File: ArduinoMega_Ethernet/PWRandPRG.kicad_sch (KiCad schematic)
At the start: 71 parts, among them J1 RJ45_Amphenol_RJMG1BD3B8K1ANR, J11 Micro_SD_Card_Det_Hirose_DM3AT, J9 PROGRAM_POWER_USBC, U2 CH340C, U3 ISM330DHCX, U4 W5500, U5 LM3281, U6 74HC244, U7 SE050C2HQ1, Y2 25Mhz

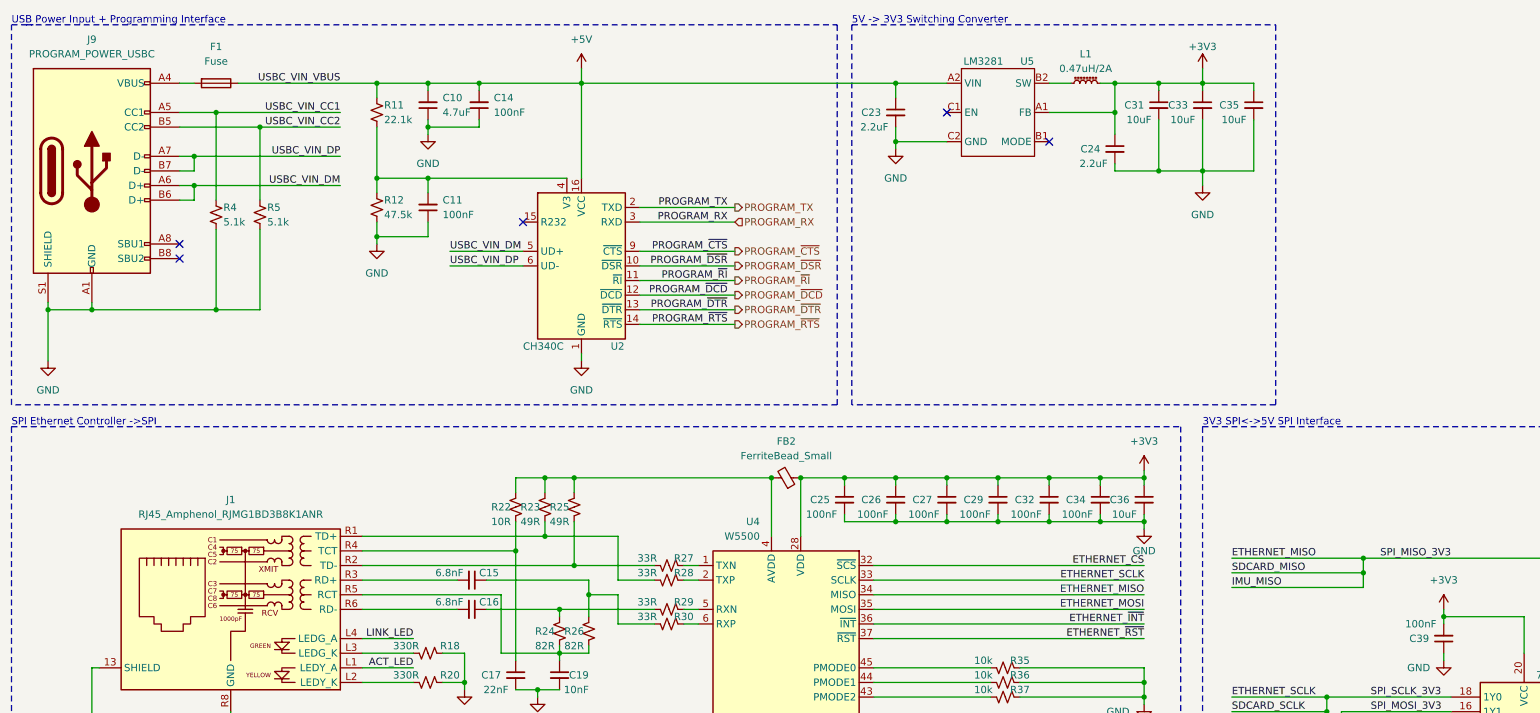
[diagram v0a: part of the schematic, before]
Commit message: add usb protection, fix ioref
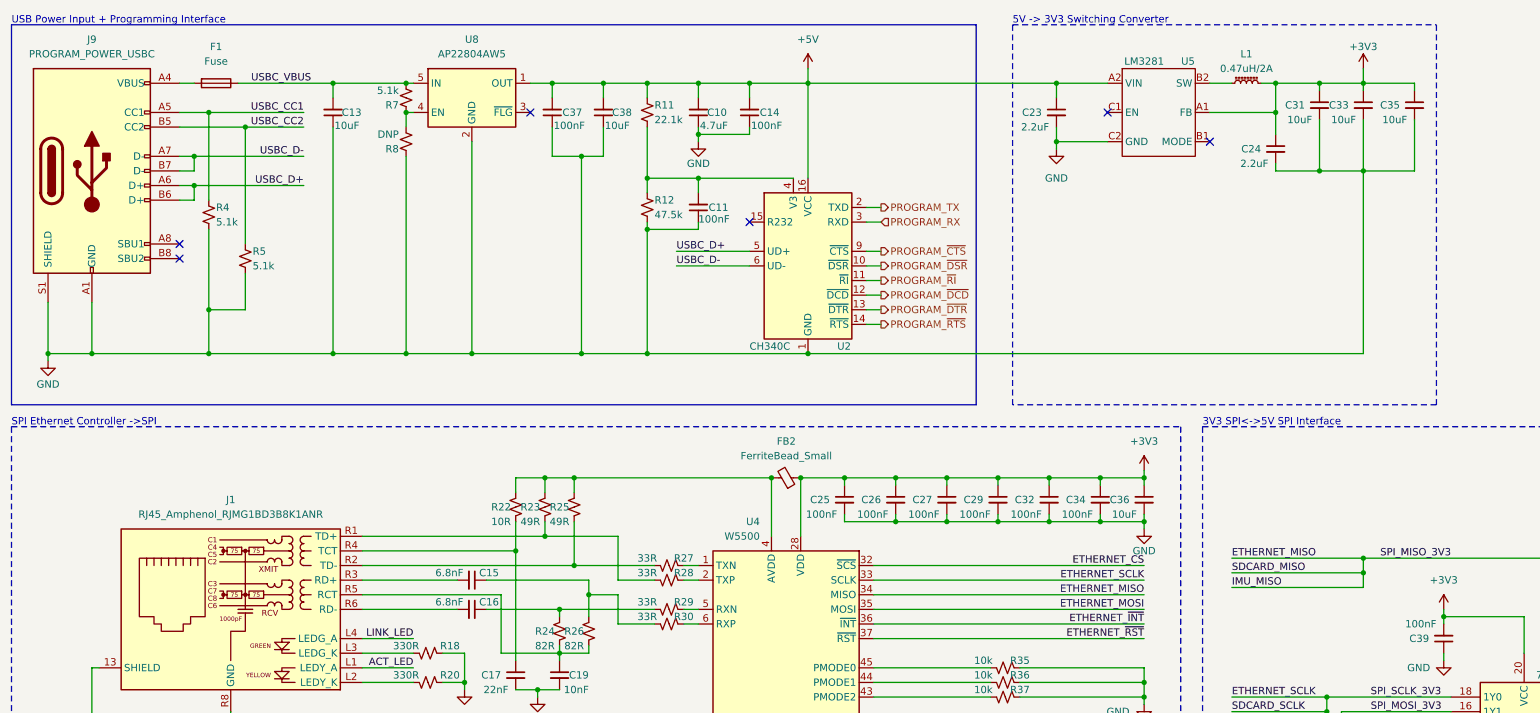
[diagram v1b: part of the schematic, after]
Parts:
- added C13, C38: 10uF, Capacitor_SMD:C_0805_2012Metric_Pad1.18x1.45mm_HandSolder, symbol Device:C_Small
- added C37: 100nF, Capacitor_SMD:C_0603_1608Metric, symbol Device:C_Small
- added R7: 5.1k, Resistor_SMD:R_0603_1608Metric, symbol Device:R_Small_US
- added R8: DNP, Resistor_SMD:R_0603_1608Metric, symbol Device:R_Small_US
- added U8: AP22804AW5, Package_TO_SOT_SMD:SOT-23-5, symbol Power_Management:AP22804AW5
- C31, C33, C35, C36: footprint Capacitor_SMD:C_1206_3216Metric -> Capacitor_SMD:C_0805_2012Metric_Pad1.18x1.45mm_HandSolder
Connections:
- net +5V: now also C37.2, C38.2, U8.1 (OUT); no longer F1.1
- net GND: now also C13.1, C37.1, C38.1, R8.2, U8.2 (GND)
- net USBC_VIN_CC1 renamed USBC_CC1
- net USBC_VIN_CC2 renamed USBC_CC2
- net USBC_VIN_DM renamed USBC_D+
- net USBC_VIN_DP renamed USBC_D-
- new net: R7.2, R8.1, U8.4 (EN)
- new net USBC_VBUS: C13.2, F1.1, R7.1, U8.5 (IN)
- no-connect marks 18 -> 19
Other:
- moved on the sheet: C10, C11, C14, C23, C24, C31, C33, C35, L1, R11, R12, R4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

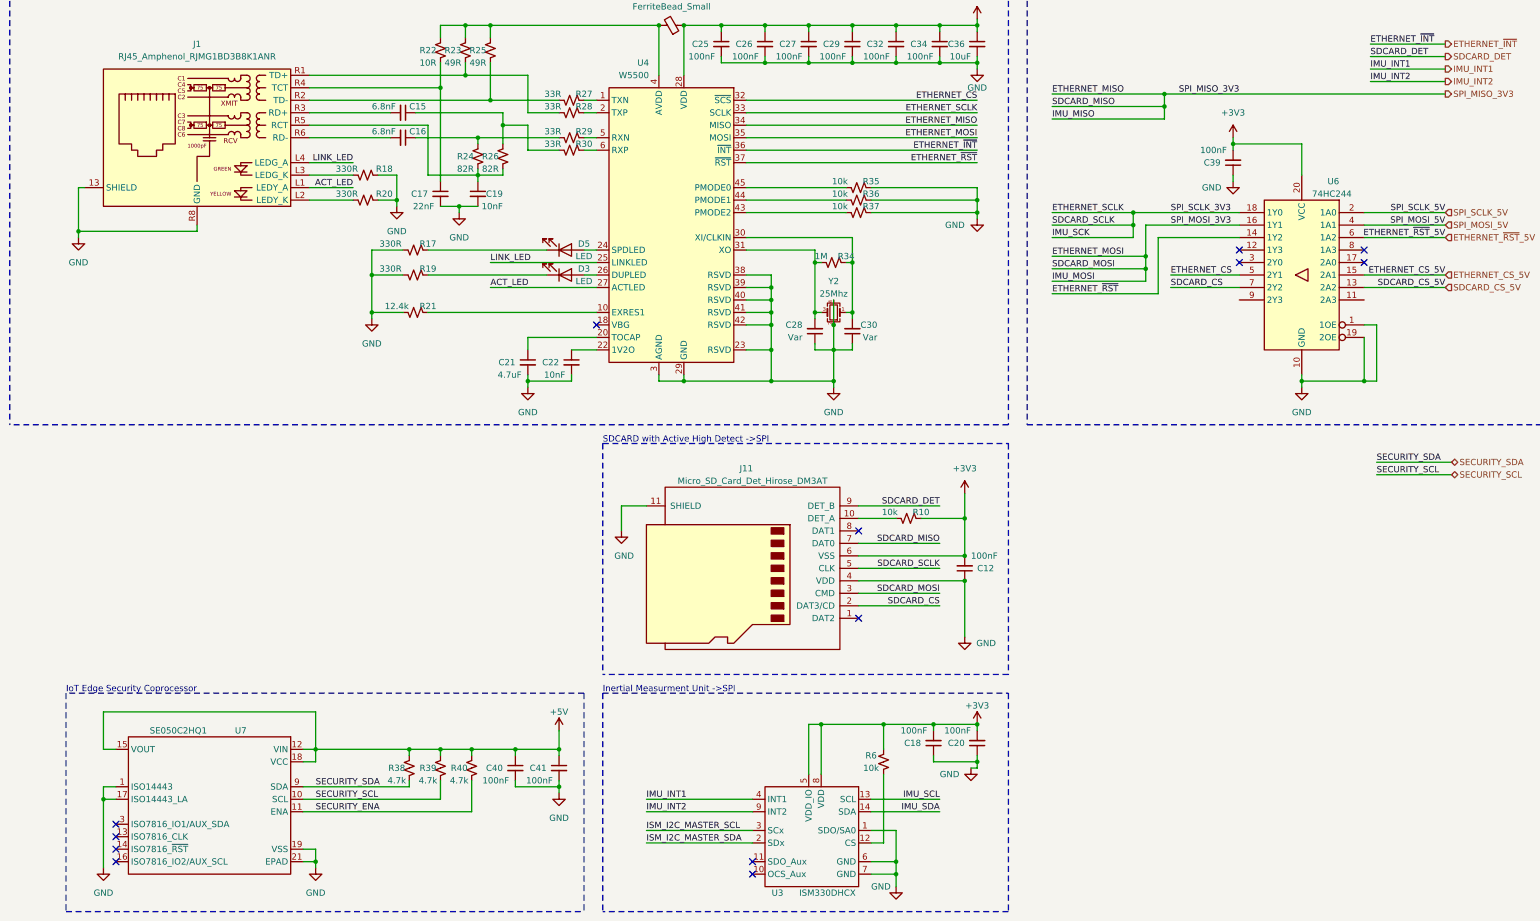
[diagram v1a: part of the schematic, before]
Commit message: Fix IMU I2C, add SD Detect, Fix IoT CoPro Power
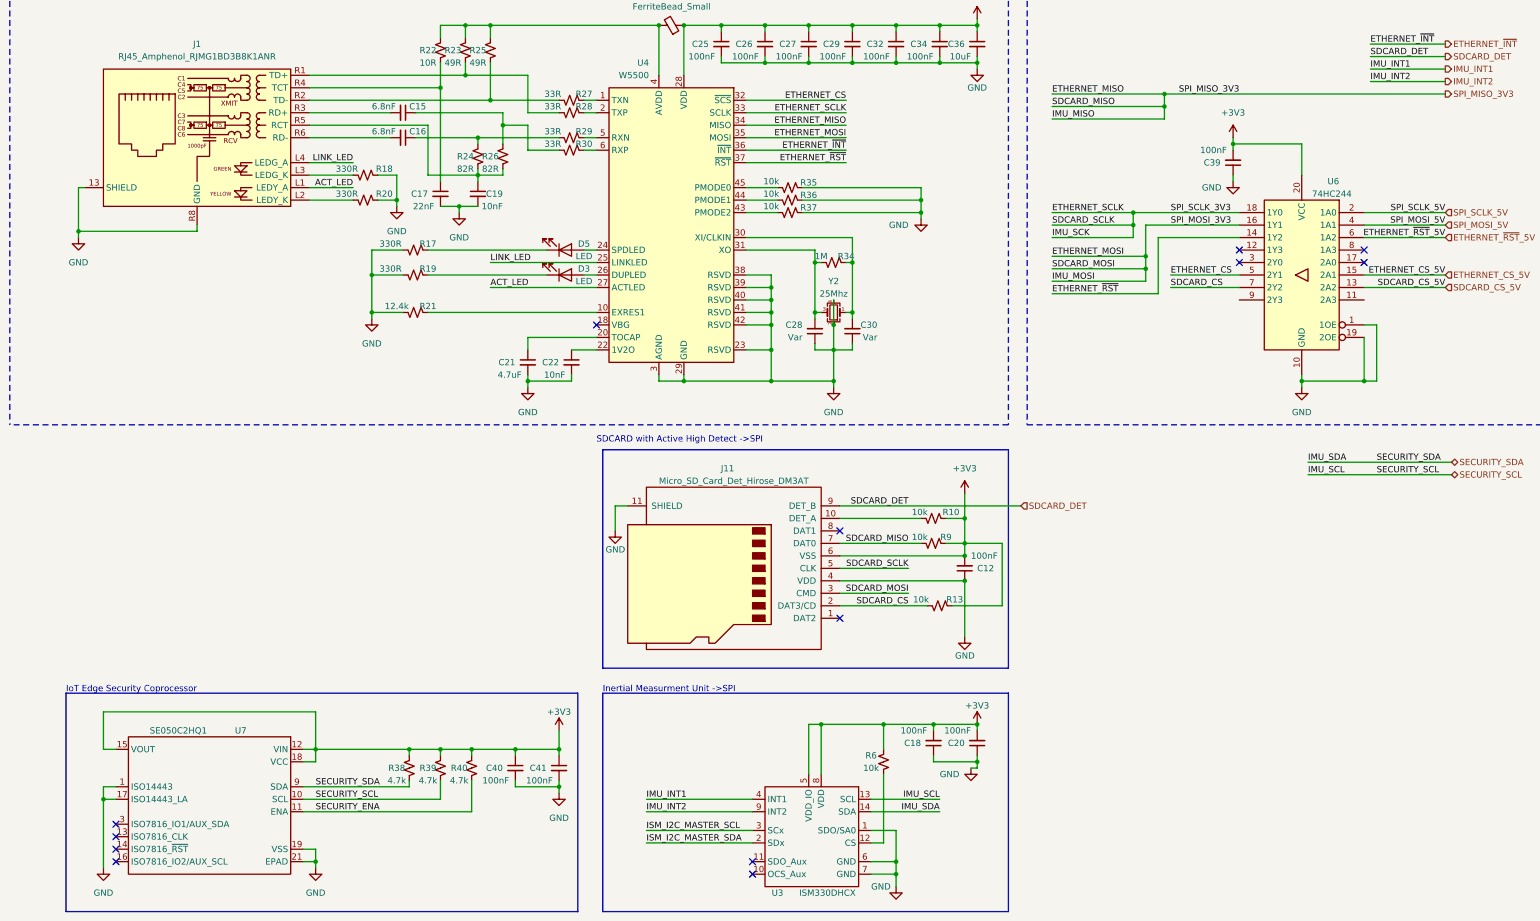
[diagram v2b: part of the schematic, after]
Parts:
- added R13, R9: 10k, Resistor_SMD:R_0603_1608Metric, symbol Device:R_Small_US
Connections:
- net IMU_SCL is gone; now on net SECURITY_SCL: U3.13 (SCL)
- net IMU_SDA is gone; now on net SECURITY_SDA: U3.14 (SDA)
- net +3V3: now also C40.1, C41.1, R38.1, R39.1, R40.1, U7.12 (VIN), U7.15 (VOUT), U7.18 (VCC), R13.1, R9.1
- net +5V: no longer C40.1, C41.1, R38.1, R39.1, R40.1, U7.12 (VIN), U7.15 (VOUT), U7.18 (VCC)
- net SDCARD_CS: now also R13.2
- net SPI_MISO_3V3: now also R9.2
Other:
- moved on the sheet: J11, R10, R35, R36, R37

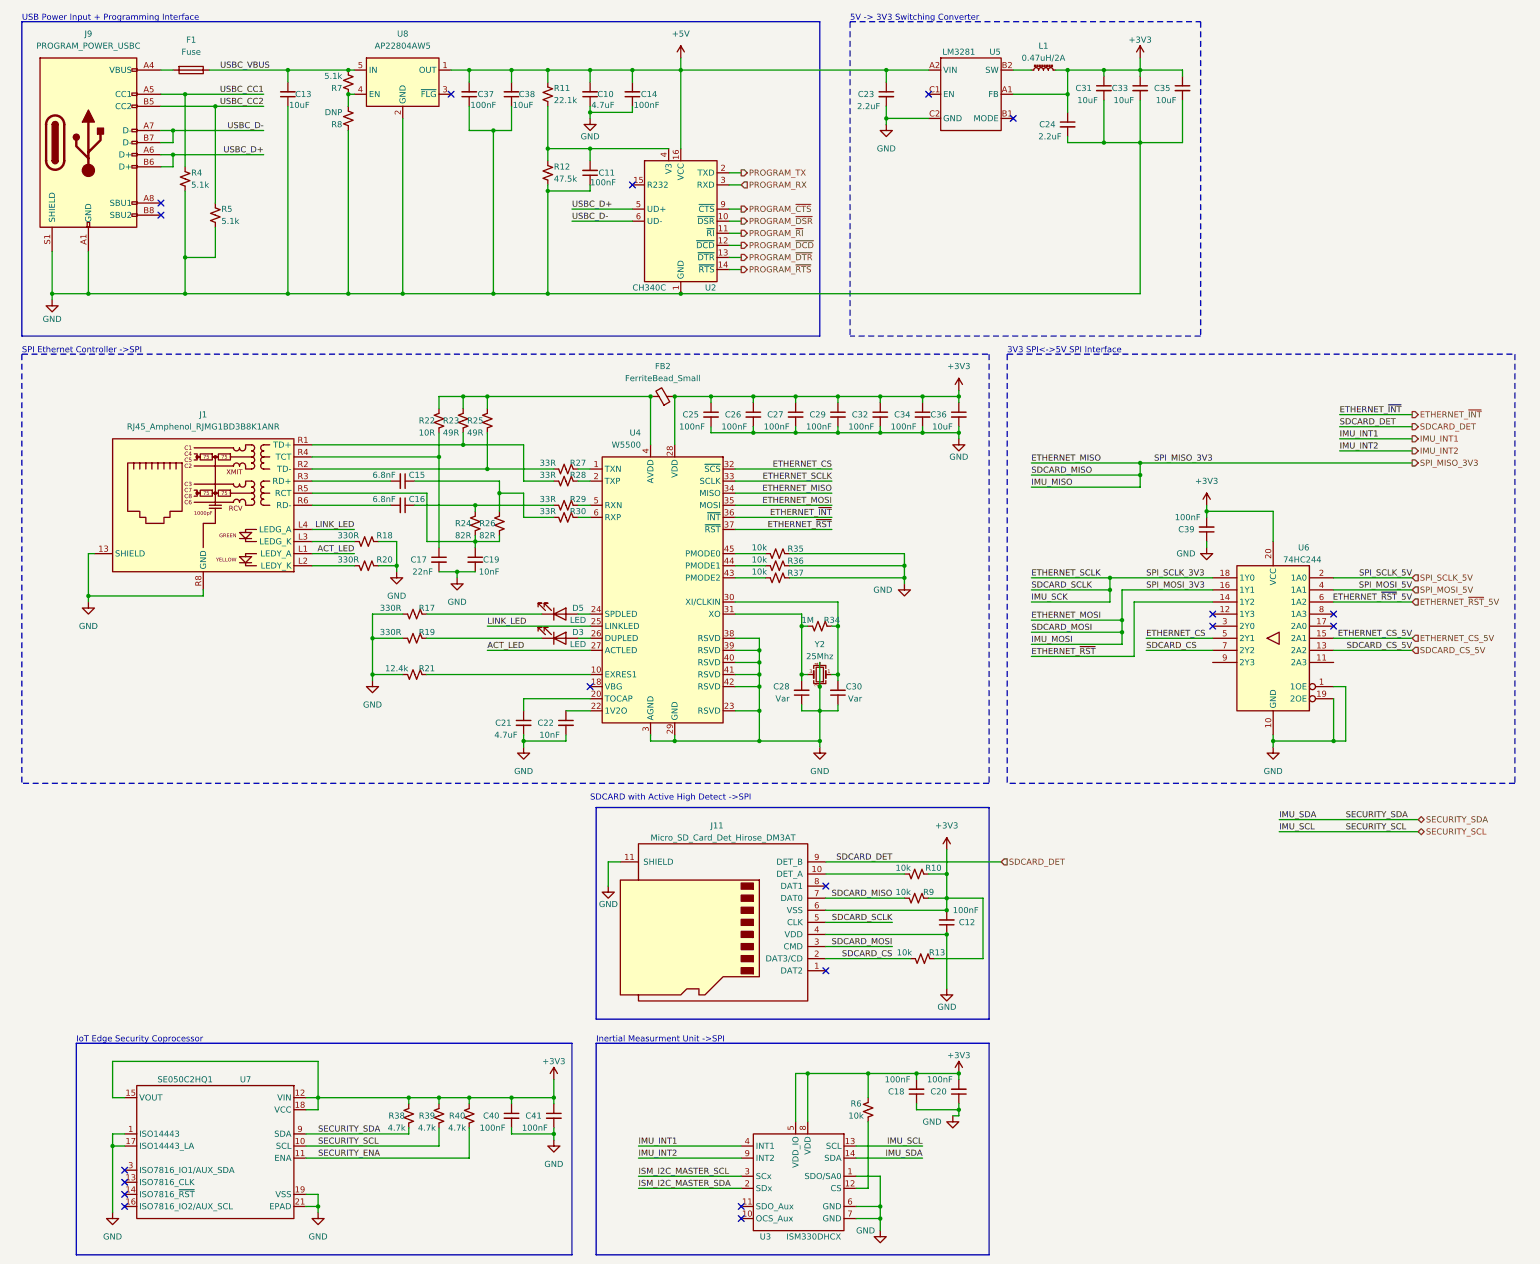
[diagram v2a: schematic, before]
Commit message: configurable io jumpers
configurable io jumpers
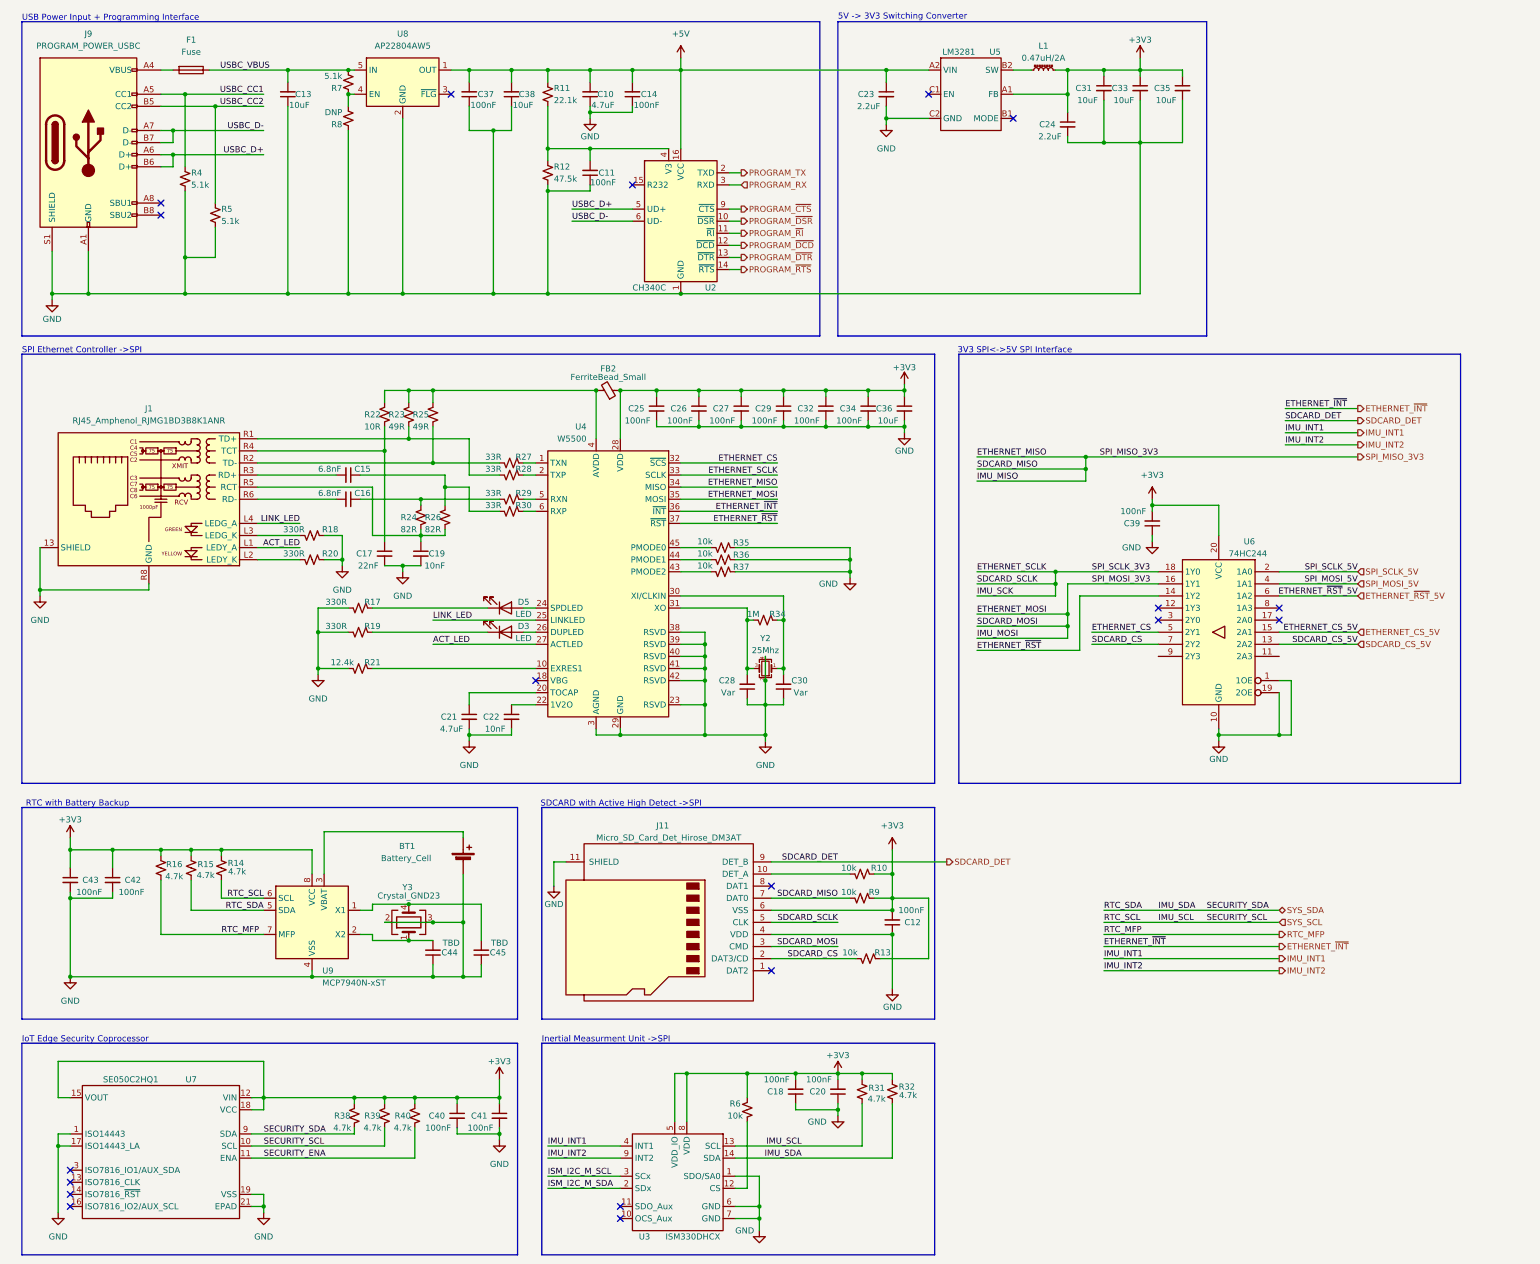
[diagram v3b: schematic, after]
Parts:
- added BT1: Battery_Cell, Connector_JST:JST_PH_B2B-PH-K_1x02_P2.00mm_Vertical, symbol Device:Battery_Cell
- added C42, C43: 100nF, Capacitor_SMD:C_0603_1608Metric, symbol Device:C_Small
- added C44, C45: TBD, Capacitor_SMD:C_0603_1608Metric, symbol Device:C_Small
- added R14, R15, R16, R31, R32: 4.7k, Resistor_SMD:R_0603_1608Metric, symbol Device:R_Small_US
- added U9: MCP7940N-xST, Package_SO:MSOP-8_3x3mm_P0.65mm, symbol Timer_RTC:MCP7940N-xST
- added Y3: Crystal_GND23, Crystal:Crystal_SMD_3225-4Pin_3.2x2.5mm_HandSoldering, symbol Device:Crystal_GND23
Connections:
- net +3V3: now also C42.1, C43.1, R14.1, R15.1, R16.1, R31.1, R32.1, U9.8 (VCC)
- net GND: now also BT1.2 (-), C42.2, C43.2, C44.1, C45.1, U9.4 (VSS), Y3.2, Y3.3
- net ISM_I2C_MASTER_SCL renamed ISM_I2C_M_SCL
- net ISM_I2C_MASTER_SDA renamed ISM_I2C_M_SDA
- net SECURITY_SCL renamed SYS_SCL
- net SYS_SCL: now also R14.2, R31.2, U9.6 (SCL)
- net SECURITY_SDA renamed SYS_SDA
- net SYS_SDA: now also R15.2, R32.2, U9.5 (SDA)
- new net: C44.2, U9.2 (X2), Y3.1
- new net: C45.2, U9.1 (X1), Y3.4
- new net: BT1.1 (+), U9.3 (VBAT)
- new net RTC_MFP: R16.2, U9.7 (MFP)
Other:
- note added: "RTC with Battery Backup"
- title: MegaEtherBoard -> Ardunio Mega with Ethernet
- moved on the sheet: C12, C15, C16, C17, C18, C19, C20, C21, C22, C25, C26, C27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
